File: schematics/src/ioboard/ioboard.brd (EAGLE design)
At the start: 27.9 x 22.2 mm, 3 parts

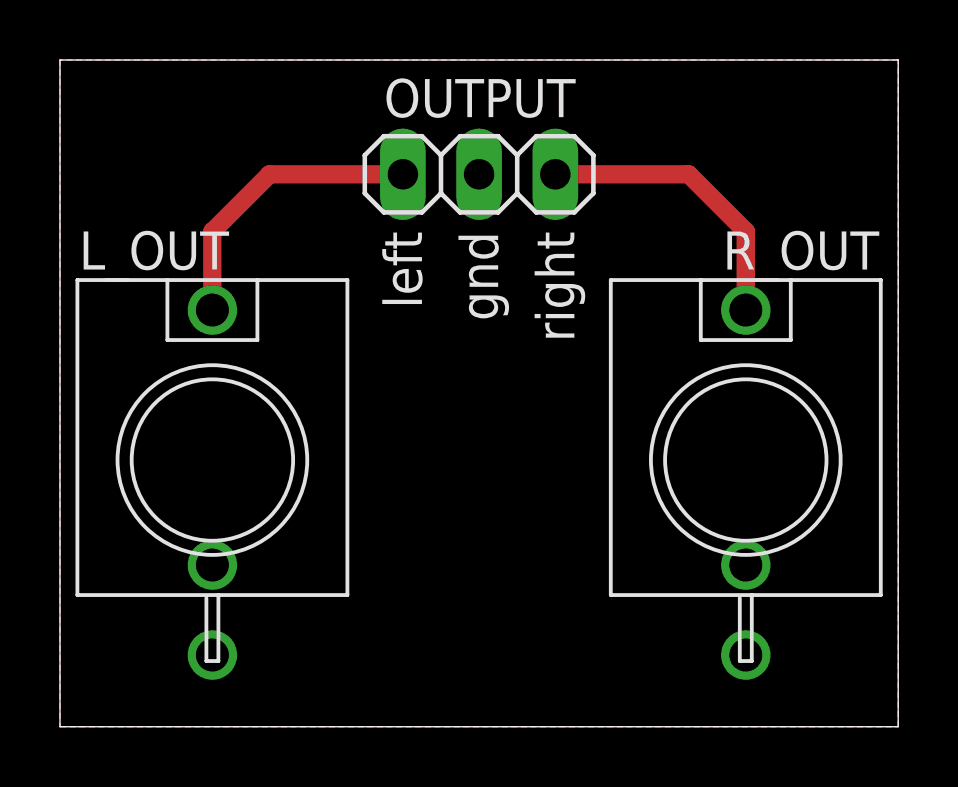
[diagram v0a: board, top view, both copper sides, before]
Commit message: Added Faceplates
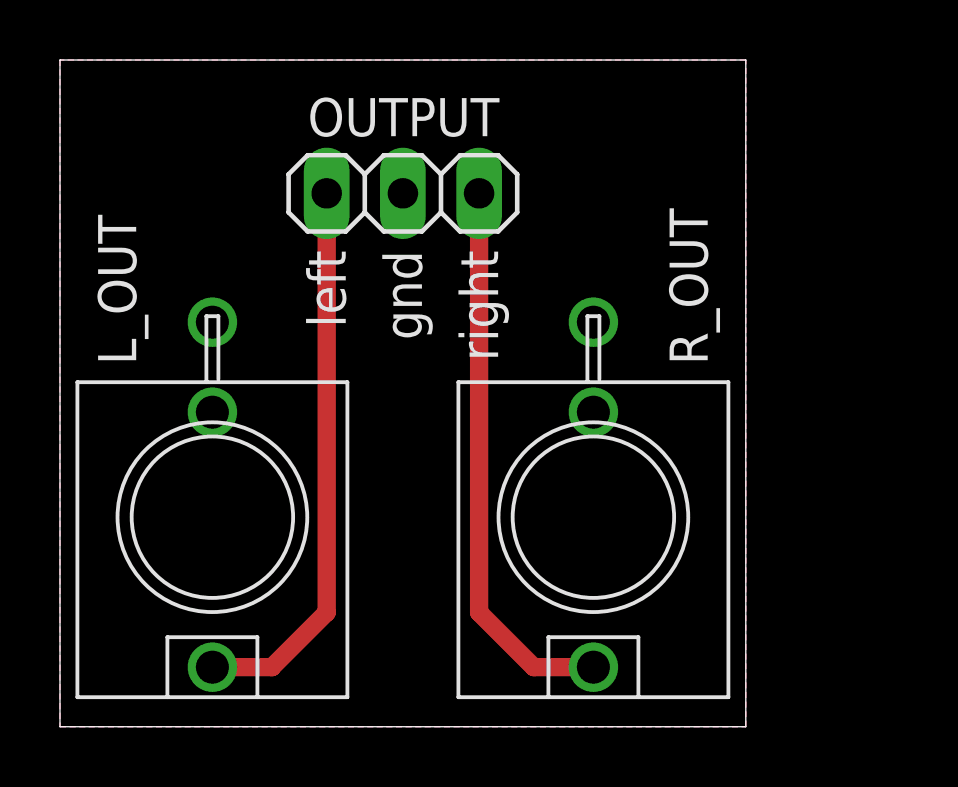
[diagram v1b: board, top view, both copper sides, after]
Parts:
- moved R_OUT 5.43 mm to (17.8, 6.99), turned to 180 degrees
- moved OUTPUT 2.62 mm to (11.4, 17.8)
- moved L_OUT 1.91 mm to (5.08, 6.99), turned to 180 degrees
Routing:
- net RIGHT_OUT: track 9.76 -> 18.5 mm
- net LEFT_OUT: track 9.76 -> 18.5 mm
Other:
- board size 27.9 x 22.2 mm -> 22.9 x 22.2 mm
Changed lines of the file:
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@@
 <board>
 <plain>
-<wire x1="0" y1="0" x2="27.94" y2="0" width="0" layer="20"/>
-<wire x1="27.94" y1="0" x2="27.94" y2="22.225" width="0" layer="20"/>
-<wire x1="27.94" y1="22.225" x2="0" y2="22.225" width="0" layer="20"/>
+<wire x1="0" y1="0" x2="22.86" y2="0" width="0" layer="20"/>
+<wire x1="22.86" y1="0" x2="22.86" y2="22.225" width="0" layer="20"/>
+<wire x1="22.86" y1="22.225" x2="0" y2="22.225" width="0" layer="20"/>
 <wire x1="0" y1="22.225" x2="0" y2="0" width="0" layer="20"/>
-<text x="10.795" y="16.51" size="1.27" layer="25" font="vector" rot="R270">left</text>
-<text x="13.335" y="16.51" size="1.27" layer="25" font="vector" rot="R270">gnd</text>
-<text x="15.875" y="16.51" size="1.27" layer="25" font="vector" rot="R270">right</text>
+<text x="8.255" y="15.875" size="1.27" layer="25" font="vector" rot="R270">left</text>
+<text x="10.795" y="15.875" size="1.27" layer="25" font="vector" rot="R270">gnd</text>
+<text x="13.335" y="15.875" size="1.27" layer="25" font="vector" rot="R270">right</text>
 </plain>
 <attributes>
@@
 </autorouter>
 <elements>
-<element name="OUTPUT" library="pinhead" library_urn="urn:adsk.eagle:library:325" package="1X03" package3d_urn="urn:adsk.eagle:package:22458/2" value="" x="13.97" y="18.415" smashed="yes" rot="R180">
-<attribute name="NAME" x="10.795" y="20.32" size="1.27" layer="25" font="vector" ratio="10"/>
-<attribute name="POPULARITY" value="92" x="13.97" y="18.415" size="1.778" layer="27" rot="R180" display="off"/>
-<attribute name="VALUE" x="17.78" y="21.59" size="1.27" layer="27" rot="R180"/>
+<element name="OUTPUT" library="pinhead" library_urn="urn:adsk.eagle:library:325" package="1X03" package3d_urn="urn:adsk.eagle:package:22458/2" value="" x="11.43" y="17.78" smashed="yes" rot="R180">
+<attribute name="NAME" x="8.255" y="19.685" size="1.27" layer="25" font="vector" ratio="10"/>
+<attribute name="POPULARITY" value="92" x="11.43" y="17.78" size="1.778" layer="27" rot="R180" display="off"/>
+<attribute name="VALUE" x="15.24" y="20.955" size="1.27" layer="27" rot="R180"/>
 </element>
-<element name="L_OUT" library="thonkiconn" package="WQP-PJ301M-12_JACK" value="" x="5.08" y="8.89" smashed="yes">
-<attribute name="NAME" x="0.635" y="15.24" size="1.27" layer="21" font="vector"/>
+<element name="L_OUT" library="thonkiconn" package="WQP-PJ301M-12_JACK" value="" x="5.08" y="6.985" smashed="yes" rot="R180">
+<attribute name="NAME" x="2.54" y="12.065" size="1.27" layer="21" font="vector" rot="R90"/>
 </element>
-<element name="R_OUT" library="thonkiconn" package="WQP-PJ301M-12_JACK" value="" x="22.86" y="8.89" smashed="yes">
-<attribute name="NAME" x="27.305" y="16.51" size="1.27" layer="21" font="vector" rot="R180"/>
+<element name="R_OUT" library="thonkiconn" package="WQP-PJ301M-12_JACK" value="" x="17.78" y="6.985" smashed="yes" rot="R180">
+<attribute name="NAME" x="21.59" y="12.065" size="1.27" layer="21" font="vector" rot="R90"/>
 </element>
 </elements>
@@
 <vertex x="0" y="22.225"/>
 <vertex x="0" y="0"/>
-<vertex x="27.94" y="0"/>
-<vertex x="27.94" y="22.225"/>
+<vertex x="22.86" y="0"/>
+<vertex x="22.86" y="22.225"/>
 </polygon>
 <polygon width="0.4064" layer="16">
 <vertex x="0" y="22.225"/>
 <vertex x="0" y="0"/>
-<vertex x="27.94" y="0"/>
-<vertex x="27.94" y="22.225"/>
+<vertex x="22.86" y="0"/>
+<vertex x="22.86" y="22.225"/>
 </polygon>
 </signal>
@@
 <contactref element="OUTPUT" pad="3"/>
 <contactref element="L_OUT" pad="P$1"/>
-<wire x1="11.43" y1="18.415" x2="6.985" y2="18.415" width="0.6096" layer="1"/>
-<wire x1="6.985" y1="18.415" x2="5.08" y2="16.51" width="0.6096" layer="1"/>
-<wire x1="5.08" y1="16.51" x2="5.08" y2="13.89" width="0.6096" layer="1"/>
+<wire x1="8.89" y1="17.78" x2="8.89" y2="3.81" width="0.6096" layer="1"/>
+<wire x1="5.08" y1="1.985" x2="7.065" y2="1.985" width="0.6096" layer="1"/>
+<wire x1="8.89" y1="3.81" x2="7.065" y2="1.985" width="0.6096" layer="1"/>
 </signal>
 <signal name="RIGHT_OUT">
 <contactref element="OUTPUT" pad="1"/>
 <contactref element="R_OUT" pad="P$1"/>
-<wire x1="22.86" y1="16.51" x2="22.86" y2="13.89" width="0.6096" layer="1"/>
-<wire x1="22.86" y1="16.51" x2="20.955" y2="18.415" width="0.6096" layer="1"/>
-<wire x1="20.955" y1="18.415" x2="16.51" y2="18.415" width="0.6096" layer="1"/>
+<wire x1="13.97" y1="17.78" x2="13.97" y2="3.81" width="0.6096" layer="1"/>
+<wire x1="17.78" y1="1.985" x2="15.795" y2="1.985" width="0.6096" layer="1"/>
+<wire x1="15.795" y1="1.985" x2="13.97" y2="3.81" width="0.6096" layer="1"/>
 </signal>
 </signals>
